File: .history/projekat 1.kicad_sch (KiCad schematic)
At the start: 224 parts, among them J1 Keyer, J2 audio_input, J3 Output signal, K1 Relay_SPST-NO_SSB (G6B-1177C(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, K2 Relay_SPST-NO_CW (G6B-1177C(-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, Q1 BC547, Q2 BC547, Q3 BC549, Q4 BC549, Q5 BC549, Q6 BC547, Q7 IRF510, Q9 BC547, SW1 on/off_12V, SW3 audio_SsbMorse_selektor, SW4 on/off_zujanje, SW5 keying_CW_SSB_selektor, SW6 selektor_modulacija, SW7 selektor_izlaza, U1 LM386, U10 OPA656UB, U11 L7806, U12 LM386, U13 OPA656UB, U14 OPA656UB, U15 OPA656UB, U2 LM358, U3 LM358, U4 LM358, U5 OPA656UB, U6 4N35, U7 OPA656UB, U8 OPA656UB, U9 OPA656UB

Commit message: rešen problem errora na pcb-u, replicirati rešenjesa J1 konektora na svim ostalim simbolima koji zadaju error.
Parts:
- removed J1: Keyer, Connector_PinHeader_2.54mm:PinHeader_1x02_P2.54mm_Vertical, symbol Connector_Audio:AudioJack2
- removed RV1: 100k, Resistor_SMD:R_1206_3216Metric_Pad1.30x1.75mm_HandSolder, symbol Device:R_Potentiometer
- added J1: Conn_01x02_Pin, Connector_PinHeader_2.54mm:PinHeader_1x02_P2.54mm_Vertical, symbol Connector:Conn_01x02_Pin
- added var_att_300mVrms2: 100k linear pot, Potentiometer_THT:Potentiometer_Bourns_3386W_Horizontal, symbol Device:R_Potentiometer
- K1, K2: footprint footprints:RELAY_G6B-1177P-ND_OMR -> (none)
- MC1496_mix2, MC1496_mod1: footprint Package_SO:SOIC-14-16_3.9x9.9mm_P1.27mm -> Package_SO:SOIC-14_3.9x8.7mm_P1.27mm
- R62: footprint Package_TO_SOT_THT:TO-220-3_Vertical -> Resistor_THT:R_Axial_DIN0516_L15.5mm_D5.0mm_P20.32mm_Horizontal
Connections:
- net GND: now also var_att_300mVrms2.3
- net at U6.2: now also J1.1 (Pin_1)
- net at SW4.2 (B): now also J1.2 (Pin_2)
- net at C27.2, U2.6 (-): now also var_att_300mVrms2.2
- net at R40.2, U2.1: now also var_att_300mVrms2.1
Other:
- note added: "rešiti footprint za otpornike na banpass-u"
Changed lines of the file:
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@@
 		)
 	)
+	(text "rešiti footprint za otpornike na banpass-u"
+		(exclude_from_sim no)
+		(at 554.99 322.072 0)
+		(effects
+			(font
+				(size 1.27 1.27)
+			)
+		)
+	)
 	(text "2nd order Chebyshev, direct coupled, shunt inductor"
 		(exclude_from_sim no)
@@
 			)
 		)
-		(property "Footprint" "footprints:RELAY_G6B-1177P-ND_OMR"
+		(property "Footprint" ""
 			(at 379.73 142.24 0)
 			(hide yes)
@@
 			)
 		)
-		(property "Footprint" "Package_TO_SOT_THT:TO-220-3_Vertical"
+		(property "Footprint" "Resistor_THT:R_Axial_DIN0516_L15.5mm_D5.0mm_P20.32mm_Horizontal"
 			(at 530.352 317.5 90)
 			(hide yes)
@@
 	)
 	(symbol
-		(lib_id "Connector_Audio:AudioJack2")
-		(at 19.05 299.72 0)
-		(unit 1)
-		(body_style 1)
-		(exclude_from_sim no)
-		(in_bom yes)
-		(on_board yes)
-		(in_pos_files yes)
-		(dnp no)
-		(fields_autoplaced yes)
-		(property "Reference" "J1"
-			(at 18.415 290.83 0)
-			(show_name no)
-			(do_not_autoplace no)
-			(effects
-				(font
-					(size 1.27 1.27)
-				)
-			)
-		)
-		(property "Value" "Keyer"
-			(at 18.415 293.37 0)
-			(show_name no)
-			(do_not_autoplace no)
-			(effects
-				(font
-					(size 1.27 1.27)
-				)
-			)
-		)
-		(property "Footprint" "Connector_PinHeader_2.54mm:PinHeader_1x02_P2.54mm_Vertical"
-			(at 19.05 299.72 0)
-			(hide yes)
-			(show_name no)
-			(do_not_autoplace no)
-			(effects
-				(font
-					(size 1.27 1.27)
-				)
-			)
-		)
-		(property "Datasheet" ""
-			(at 19.05 299.72 0)
-			(hide yes)
-			(show_name no)
-			(do_not_autoplace no)
-			(effects
-				(font
-					(size 1.27 1.27)
-				)
-			)
-		)
-		(property "Description" "Audio Jack, 2 Poles (Mono / TS)"
-			(at 19.05 299.72 0)
-			(hide yes)
-			(show_name no)
-			(do_not_autoplace no)
-			(effects
-				(font
-					(size 1.27 1.27)
-				)
-			)
-		)
-		(pin "S"
-		)
-		(pin "T"
-		)
-		(instances
-			(project "projekat 1"
-				(path "/74b4ec7a-02ca-4148-b3fb-b94fa07f486f"
-					(reference "J1")
-					(unit 1)
-				)
-			)
-		)
-	)
-	(symbol
 		(lib_id "Device:R")
 		(at 165.1 39.37 0)
@@
 	)
 	(symbol
-		(lib_id "Device:R_Potentiometer")
-		(at 55.88 223.52 0)
-		(unit 1)
-		(body_style 1)
-		(exclude_from_sim no)
-		(in_bom yes)
-		(on_board yes)
-		(in_pos_files yes)
-		(dnp no)
-		(fields_autoplaced yes)
-		(property "Reference" "RV1"
-			(at 53.34 222.2499 0)
-			(show_name no)
-			(do_not_autoplace no)
-			(effects
-				(font
-					(size 1.27 1.27)
-				)
-				(justify right)
-			)
-		)
-		(property "Value" "100k"
-			(at 53.34 224.7899 0)
-			(show_name no)
-			(do_not_autoplace no)
-			(effects
-				(font
-					(size 1.27 1.27)
-				)
-				(justify right)
-			)
-		)
-		(property "Footprint" "Resistor_SMD:R_1206_3216Metric_Pad1.30x1.75mm_HandSolder"
-			(at 55.88 223.52 0)
-			(hide yes)
-			(show_name no)
-			(do_not_autoplace no)
-			(effects
-				(font
-					(size 1.27 1.27)
-				)
-			)
-		)
-		(property "Datasheet" ""
-			(at 55.88 223.52 0)
-			(hide yes)
-			(show_name no)
-			(do_not_autoplace no)
-			(effects
-				(font
-					(size 1.27 1.27)
-				)
-			)
-		)
-		(property "Description" "Potentiometer"
-			(at 55.88 223.52 0)
-			(hide yes)
-			(show_name no)
-			(do_not_autoplace no)
-			(effects
-				(font
-					(size 1.27 1.27)
-				)
-			)
-		)
-		(property "Sim.Device" "R"
-			(at 55.88 223.52 0)
-			(hide yes)
-			(show_name no)
-			(do_not_autoplace no)
-			(effects
-				(font
-					(size 1.27 1.27)
-				)
-			)
-		)
-		(property "Sim.Type" "POT"
-			(at 55.88 223.52 0)
-			(hide yes)
-			(show_name no)
-			(do_not_autoplace no)
-			(effects
-				(font
-					(size 1.27 1.27)
-				)
-			)
-		)
-		(property "Sim.Pins" "1=r0 2=wiper 3=r1"
-			(at 55.88 223.52 0)
-			(hide yes)
-			(show_name no)
-			(do_not_autoplace no)
-			(effects
-				(font
-					(size 1.27 1.27)
-				)
-			)
-		)
-		(pin "2"
-		)
-		(pin "3"
-		)
-		(pin "1"
-		)
-		(instances
-			(project "projekat 1"
-				(path "/74b4ec7a-02ca-4148-b3fb-b94fa07f486f"
-					(reference "RV1")
-					(unit 1)
-				)
-			)
-		)
-	)
-	(symbol
 		(lib_id "Device:C")
 		(at 361.95 77.47 0)
@@
 			)
 		)
-		(property "Footprint" "Package_SO:SOIC-14-16_3.9x9.9mm_P1.27mm"
+		(property "Footprint" "Package_SO:SOIC-14_3.9x8.7mm_P1.27mm"
 			(at 130.81 132.08 0)
 			(hide yes)
@@
 			)
 		)
-		(property "Footprint" "Package_SO:SOIC-14-16_3.9x9.9mm_P1.27mm"
+		(property "Footprint" "Package_SO:SOIC-14_3.9x8.7mm_P1.27mm"
 			(at 128.27 45.72 0)
 			(hide yes)
@@
 	)
 	(symbol
+		(lib_id "Device:R_Potentiometer")
+		(at 55.88 223.52 0)
+		(unit 1)
+		(body_style 1)
+		(exclude_from_sim no)
+		(in_bom yes)
+		(on_board yes)
+		(in_pos_files yes)
+		(dnp no)
+		(property "Reference" "var_att_300mVrms2"
+			(at 49.53 223.52 90)
+			(show_name no)
+			(do_not_autoplace no)
+			(effects
+				(font
+					(size 1.27 1.27)
+				)
+			)
+		)
+		(property "Value" "100k linear pot"
+			(at 52.07 223.52 90)
+			(show_name no)
+			(do_not_autoplace no)
+			(effects
+				(font
+					(size 1.27 1.27)
+				)
+			)
+		)
+		(property "Footprint" "Potentiometer_THT:Potentiometer_Bourns_3386W_Horizontal"
+			(at 55.88 223.52 0)
+			(hide yes)
+			(show_name no)
+			(do_not_autoplace no)
+			(effects
+				(font
+					(size 1.27 1.27)
+				)
+			)
+		)
+		(property "Datasheet" ""
+			(at 55.88 223.52 0)
+			(hide yes)
+			(show_name no)
+			(do_not_autoplace no)
+			(effects
+				(font
+					(size 1.27 1.27)
+				)
+			)
+		)
+		(property "Description" "Potentiometer"
+			(at 55.88 223.52 0)
+			(hide yes)
+			(show_name no)
+			(do_not_autoplace no)
+			(effects
+				(font
+					(size 1.27 1.27)
+				)
+			)
+		)
+		(property "Sim.Device" "R"
+			(at 55.88 223.52 0)
+			(hide yes)
+			(show_name no)
+			(do_not_autoplace no)
+			(effects
+				(font
+					(size 1.27 1.27)
+				)
+			)
+		)
+		(property "Sim.Type" "POT"
+			(at 55.88 223.52 0)
+			(hide yes)
+			(show_name no)
+			(do_not_autoplace no)
+			(effects
+				(font
+					(size 1.27 1.27)
+				)
+			)
+		)
+		(property "Sim.Pins" "1=r0 2=wiper 3=r1"
+			(at 55.88 223.52 0)
+			(hide yes)
+			(show_name no)
+			(do_not_autoplace no)
+			(effects
+				(font
+					(size 1.27 1.27)
+				)
+			)
+		)
+		(pin "3"
+		)
+		(pin "2"
+		)
+		(pin "1"
+		)
+		(instances
+			(project "projekat 1"
+				(path "/74b4ec7a-02ca-4148-b3fb-b94fa07f486f"
+					(reference "var_att_300mVrms2")
+					(unit 1)
+				)
+			)
+		)
+	)
+	(symbol
 		(lib_id "Device:R")
 		(at 284.48 77.47 0)
@@
 	)
 	(symbol
+		(lib_id "Connector:Conn_01x02_Pin")
+		(at 19.05 297.18 0)
+		(unit 1)
+		(body_style 1)
+		(exclude_from_sim no)
+		(in_bom yes)
+		(on_board yes)
+		(in_pos_files yes)
+		(dnp no)
+		(fields_autoplaced yes)
+		(property "Reference" "J1"
+			(at 19.685 292.1 0)
+			(show_name no)
+			(do_not_autoplace no)
+			(effects
+				(font
+					(size 1.27 1.27)
+				)
+			)
+		)
+		(property "Value" "Conn_01x02_Pin"
+			(at 19.685 294.64 0)
+			(show_name no)
+			(do_not_autoplace no)
+			(effects
+				(font
+					(size 1.27 1.27)
+				)
+			)
+		)
+		(property "Footprint" "Connector_PinHeader_2.54mm:PinHeader_1x02_P2.54mm_Vertical"
+			(at 19.05 297.18 0)
+			(hide yes)
+			(show_name no)
+			(do_not_autoplace no)
+			(effects
+				(font
+					(size 1.27 1.27)
+				)
+			)
+		)
+		(property "Datasheet" ""
+			(at 19.05 297.18 0)
+			(hide yes)
+			(show_name no)
+			(do_not_autoplace no)
+			(effects
+				(font
+					(size 1.27 1.27)
+				)
+			)
+		)
+		(property "Description" "Generic connector, single row, 01x02, script generated"
+			(at 19.05 297.18 0)
+			(hide yes)
+			(show_name no)
+			(do_not_autoplace no)
+			(effects
+				(font
+					(size 1.27 1.27)
+				)
+			)
+		)
+		(pin "2"
+		)
+		(pin "1"
+		)
+		(instances
+			(project "projekat 1"
+				(path "/74b4ec7a-02ca-4148-b3fb-b94fa07f486f"
+					(reference "J1")
+					(unit 1)
+				)
+			)
+		)
+	)
+	(symbol
 		(lib_id "Device:L")
 		(at 494.03 311.15 90)
@@
 			)
 		)
-		(property "Footprint" "footprints:RELAY_G6B-1177P-ND_OMR"
+		(property "Footprint" ""
 			(at 346.71 142.24 0)
 			(hide yes)

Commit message: organizovan layout tone generation, signal input, headphone interface. Promenjen net na LE diodi u 12V_supply_1 i dodat otpornik od 500 oma.
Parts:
- removed J2: audio_input, Connector_PinHeader_2.54mm:PinHeader_1x02_P2.54mm_Vertical, symbol Connector_Audio:AudioJack2
- removed TS_6.35mm1: head_out, Connector_PinHeader_2.54mm:PinHeader_1x01_P2.54mm_Vertical, symbol Connector_Audio:AudioJack2
- added J2, J4: Conn_01x02_Pin, Connector_PinHeader_2.54mm:PinHeader_1x02_P2.54mm_Vertical, symbol Connector:Conn_01x02_Pin
- added R63: 500, Resistor_SMD:R_1206_3216Metric_Pad1.30x1.75mm_HandSolder, symbol Device:R
- BZ1: footprint Connector_PinHeader_2.54mm:PinHeader_1x01_P2.54mm_Vertical -> Connector_PinHeader_2.54mm:PinHeader_1x02_P2.54mm_Vertical
- SW4: footprint Connector_PinHeader_2.54mm:PinHeader_1x01_P2.54mm_Vertical -> Connector_PinHeader_2.54mm:PinHeader_1x03_P2.54mm_Vertical
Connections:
- net 12V_supply_1: now also R63.1
- net GND: now also J2.1 (Pin_1), J4.2 (Pin_2)
- net VCC: no longer D1.2 (A)
- net at C37.2: now also J2.2 (Pin_2)
- net at C38.1: now also J4.1 (Pin_1)
- new net: D1.2 (A), R63.2

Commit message: Izvršena prva korekcija layout-a tone generation, signal input, headphone interfacebloka, zamenjen footprint lm358 u SOIC-8. U sledećoj iteraciji dodati više slojeva, trace-ve koji su ispod komponenata spustiti u donji sloj, pregledati trace-ove
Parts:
- R63: value 500 -> 220
- U2, U3, U4: footprint Package_DIP:DIP-8_W7.62mm_LongPads -> Package_SO:SOIC-8_3.9x4.9mm_P1.27mm
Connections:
- net +6V: now also R63.1
- net 12V_supply_1: no longer R63.1
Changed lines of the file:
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@@
 	)
 	(label "12V_supply_1"
-		(at 25.4 274.32 0)
-		(effects
-			(font
-				(size 1.27 1.27)
-				(thickness 0.254)
-				(bold yes)
-				(italic yes)
-			)
-			(justify left bottom)
-		)
-	)
-	(label "12V_supply_1"
 		(at 210.82 320.04 270)
 		(effects
@@
 			)
 		)
-		(property "Footprint" "Package_DIP:DIP-8_W7.62mm_LongPads"
+		(property "Footprint" "Package_SO:SOIC-8_3.9x4.9mm_P1.27mm"
 			(at 114.3 242.57 0)
 			(hide yes)
@@
 			)
 		)
-		(property "Footprint" "Package_DIP:DIP-8_W7.62mm_LongPads"
+		(property "Footprint" "Package_SO:SOIC-8_3.9x4.9mm_P1.27mm"
 			(at 237.49 227.33 0)
 			(hide yes)
@@
 			)
 		)
-		(property "Footprint" "Package_DIP:DIP-8_W7.62mm_LongPads"
+		(property "Footprint" "Package_SO:SOIC-8_3.9x4.9mm_P1.27mm"
 			(at 149.86 281.94 0)
 			(hide yes)
@@
 			)
 		)
-		(property "Footprint" "Package_DIP:DIP-8_W7.62mm_LongPads"
+		(property "Footprint" "Package_SO:SOIC-8_3.9x4.9mm_P1.27mm"
 			(at 246.38 227.33 0)
 			(hide yes)
@@
 	)
 	(symbol
+		(lib_id "power:+6V")
+		(at 25.4 274.32 0)
+		(unit 1)
+		(body_style 1)
+		(exclude_from_sim no)
+		(in_bom yes)
+		(on_board yes)
+		(in_pos_files yes)
+		(dnp no)
+		(property "Reference" "#PWR016"
+			(at 25.4 278.13 0)
+			(hide yes)
+			(show_name no)
+			(do_not_autoplace no)
+			(effects
+				(font
+					(size 1.27 1.27)
+				)
+			)
+		)
+		(property "Value" "+6V"
+			(at 25.4 270.002 0)
+			(show_name no)
+			(do_not_autoplace no)
+			(effects
+				(font
+					(size 1.27 1.27)
+				)
+			)
+		)
+		(property "Footprint" ""
+			(at 25.4 274.32 0)
+			(hide yes)
+			(show_name no)
+			(do_not_autoplace no)
+			(effects
+				(font
+					(size 1.27 1.27)
+				)
+			)
+		)
+		(property "Datasheet" ""
+			(at 25.4 274.32 0)
+			(hide yes)
+			(show_name no)
+			(do_not_autoplace no)
+			(effects
+				(font
+					(size 1.27 1.27)
+				)
+			)
+		)
+		(property "Description" "Power symbol creates a global label with name \"+6V\""
+			(at 25.4 274.32 0)
+			(hide yes)
+			(show_name no)
+			(do_not_autoplace no)
+			(effects
+				(font
+					(size 1.27 1.27)
+				)
+			)
+		)
+		(pin "1"
+		)
+		(instances
+			(project "projekat 1"
+				(path "/74b4ec7a-02ca-4148-b3fb-b94fa07f486f"
+					(reference "#PWR016")
+					(unit 1)
+				)
+			)
+		)
+	)
+	(symbol
 		(lib_id "Device:C_Polarized_US")
 		(at 110.49 72.39 0)
@@
 			)
 		)
-		(property "Footprint" "Package_DIP:DIP-8_W7.62mm_LongPads"
+		(property "Footprint" "Package_SO:SOIC-8_3.9x4.9mm_P1.27mm"
 			(at 69.85 226.06 0)
 			(hide yes)
@@
 			)
 		)
-		(property "Footprint" "Package_DIP:DIP-8_W7.62mm_LongPads"
+		(property "Footprint" "Package_SO:SOIC-8_3.9x4.9mm_P1.27mm"
 			(at 41.91 226.06 0)
 			(hide yes)
@@
 			)
 		)
-		(property "Footprint" "Package_DIP:DIP-8_W7.62mm_LongPads"
+		(property "Footprint" "Package_SO:SOIC-8_3.9x4.9mm_P1.27mm"
 			(at 172.72 266.7 0)
 			(hide yes)
@@
 			)
 		)
-		(property "Value" "500"
+		(property "Value" "220"
 			(at 27.94 279.3999 0)
 			(show_name no)
@@
 			)
 		)
-		(property "Footprint" "Package_DIP:DIP-8_W7.62mm_LongPads"
+		(property "Footprint" "Package_SO:SOIC-8_3.9x4.9mm_P1.27mm"
 			(at 157.48 213.36 0)
 			(hide yes)
@@
 		(in_pos_files yes)
 		(dnp no)
-		(fields_autoplaced yes)
 		(property "Reference" "#PWR03"
 			(at 361.95 72.39 0)
@@
 		)
 		(property "Value" "+6V"
-			(at 361.95 63.5 0)
+			(at 361.95 64.262 0)
 			(show_name no)
 			(do_not_autoplace no)
@@
 			)
 		)
-		(property "Footprint" "Package_DIP:DIP-8_W7.62mm_LongPads"
+		(property "Footprint" "Package_SO:SOIC-8_3.9x4.9mm_P1.27mm"
 			(at 228.6 227.33 0)
 			(hide yes)

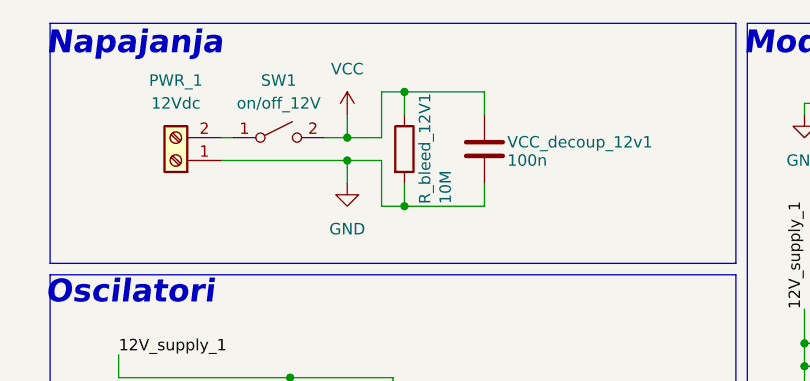
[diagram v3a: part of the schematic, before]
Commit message: dorađen layout pcb-a, dodati novi layeri, sprovedene vije.
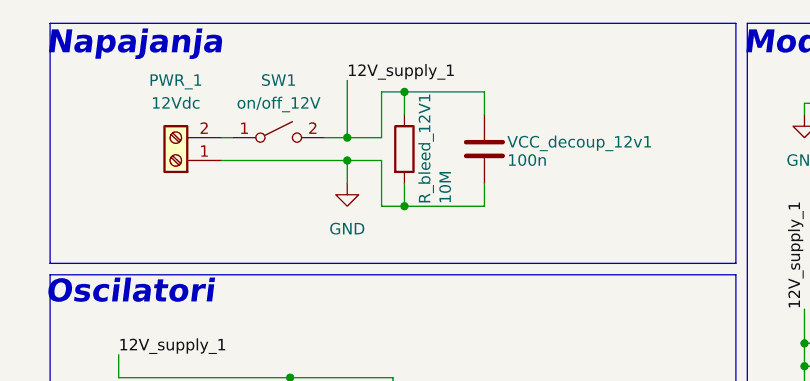
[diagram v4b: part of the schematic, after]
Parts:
- PWR_1, SW1: footprint Connector_PinHeader_2.54mm:PinHeader_1x01_P2.54mm_Vertical -> Connector_PinHeader_2.54mm:PinHeader_1x02_P2.54mm_Vertical
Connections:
- net 12V_supply_1: now also R_bleed_12V1.1, SW1.2 (B), VCC_decoup_12v1.1
- net VCC: no longer R_bleed_12V1.1, SW1.2 (B), VCC_decoup_12v1.1
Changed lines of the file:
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@@
 	(wire
 		(pts
+			(xy 45.72 19.05) (xy 45.72 25.4)
+		)
+		(stroke
+			(width 0)
+			(type default)
+		)
+	)
+	(wire
+		(pts
 			(xy 355.6 125.73) (xy 358.14 125.73)
 		)
@@
 	(wire
 		(pts
-			(xy 45.72 25.4) (xy 45.72 22.86)
-		)
-		(stroke
-			(width 0)
-			(type default)
-		)
-	)
-	(wire
-		(pts
 			(xy 161.29 33.02) (xy 161.29 43.18)
 		)
@@
 		)
 	)
+	(label "12V_supply_1"
+		(at 45.72 19.05 0)
+		(effects
+			(font
+				(size 1.27 1.27)
+			)
+			(justify left bottom)
+		)
+	)
 	(label "output_amplification_cw"
 		(at 350.52 248.92 180)
@@
 			)
 		)
-		(property "Footprint" "Connector_PinHeader_2.54mm:PinHeader_1x01_P2.54mm_Vertical"
+		(property "Footprint" "Connector_PinHeader_2.54mm:PinHeader_1x02_P2.54mm_Vertical"
 			(at 38.1 25.4 0)
 			(hide yes)
@@
 			)
 		)
-		(property "Footprint" "Connector_PinHeader_2.54mm:PinHeader_1x01_P2.54mm_Vertical"
+		(property "Footprint" "Connector_PinHeader_2.54mm:PinHeader_1x02_P2.54mm_Vertical"
 			(at 26.67 27.94 0)
 			(hide yes)
@@
 					(unit 1)
 				)
-			)
-		)
-	)
-	(symbol
-		(lib_id "power:VCC")
-		(at 45.72 22.86 0)
-		(unit 1)
-		(body_style 1)
-		(exclude_from_sim no)
-		(in_bom yes)
-		(on_board yes)
-		(in_pos_files yes)
-		(dnp no)
-		(fields_autoplaced yes)
-		(property "Reference" "#PWR013"
-			(at 45.72 26.67 0)
-			(hide yes)
-			(show_name no)
-			(do_not_autoplace no)
-			(effects
-				(font
-					(size 1.27 1.27)
-				)
-			)
-		)
-		(property "Value" "VCC"
-			(at 45.72 17.78 0)
-			(show_name no)
-			(do_not_autoplace no)
-			(effects
-				(font
-					(size 1.27 1.27)
-				)
-			)
-		)
-		(property "Footprint" ""
-			(at 45.72 22.86 0)
-			(hide yes)
-			(show_name no)
-			(do_not_autoplace no)
-			(effects
-				(font
-					(size 1.27 1.27)
-				)
-			)
-		)
-		(property "Datasheet" ""
-			(at 45.72 22.86 0)
-			(hide yes)
-			(show_name no)
-			(do_not_autoplace no)
-			(effects
-				(font
-					(size 1.27 1.27)
-				)
-			)
-		)
-		(property "Description" "Power symbol creates a global label with name \"VCC\""
-			(at 45.72 22.86 0)
-			(hide yes)
-			(show_name no)
-			(do_not_autoplace no)
-			(effects
-				(font
-					(size 1.27 1.27)
-				)
-			)
-		)
-		(pin "1"
-		)
-		(instances
-			(project "projekat 1"
-				(path "/74b4ec7a-02ca-4148-b3fb-b94fa07f486f"
-					(reference "#PWR013")
-					(unit 1)
-				)

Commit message: Dodati decoupling koncdnzatori na sve blokove i operacione, obrisan gornji layer bakra, sve vije prebačene na through, drc zadaje erore da su netovi šortivani
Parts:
- added VCC_decoup_12v2, VCC_decoup_12v3, VCC_decoup_12v4, VCC_decoup_12v5, VCC_decoup_12v6, VCC_decoup_12v7, VCC_decoup_12v8, VCC_decoup_12v9: 100n, Capacitor_SMD:C_1206_3216Metric, symbol Device:C
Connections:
- net 12V_supply_1: now also VCC_decoup_12v2.1, VCC_decoup_12v3.1, VCC_decoup_12v5.1, VCC_decoup_12v6.1, VCC_decoup_12v7.1, VCC_decoup_12v8.1, VCC_decoup_12v9.1
- net 12V_supply_CW: now also VCC_decoup_12v4.1
- net GND: now also VCC_decoup_12v2.2, VCC_decoup_12v3.2, VCC_decoup_12v4.2, VCC_decoup_12v5.2, VCC_decoup_12v6.2, VCC_decoup_12v7.2, VCC_decoup_12v8.2, VCC_decoup_12v9.2

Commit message: dodati footprinti za promenljive kondenzatore (proveriti da li su adekvatni)
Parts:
- removed C1, C2, C41, C42: 100p, Capacitor_SMD:C_1206_3216Metric, symbol Device:C
- removed C39, C40, decoup_+6V1: 100n, Capacitor_SMD:C_1206_3216Metric, symbol Device:C
- removed C_d_op1, C_d_op2, C_d_op3, C_d_op4, C_d_op5: 0,1u, Capacitor_SMD:C_1206_3216Metric, symbol Device:C
- removed C_d_op_2_1, C_d_op_2_2: 10n, Capacitor_SMD:C_1206_3216Metric, symbol Device:C
- removed C_dc1, C_dc2, C_lo_vfo1: 10nF, Capacitor_SMD:C_1206_3216Metric, symbol Device:C
- removed J3: Output signal, Connector_PinHeader_2.54mm:PinHeader_1x02_P2.54mm_Vertical, symbol Connector:Screw_Terminal_01x02
- removed K1: Relay_SPST-NO_SSB (G6B-1177C(-FD)-ND-US), symbol Relay:Relay_SPST-NO
- removed K2: Relay_SPST-NO_CW (G6B-1177C(-FD)-ND-US), symbol Relay:Relay_SPST-NO
- removed L1, L11, L5, L7: 1.6u, Inductor_SMD:L_1206_3216Metric, symbol Device:L
- removed L10, L3, L6, L8: 3.9u, Inductor_SMD:L_1206_3216Metric, symbol Device:L
- removed L4, L9: 750n, Capacitor_SMD:C_1206_3216Metric, symbol Device:L
- removed Q7: IRF510, Package_TO_SOT_THT:TO-220-3_Vertical, symbol Transistor_FET:IRF540N
- removed Q9: BC547, Package_TO_SOT_THT:TO-92_Inline, symbol Transistor_BJT:BC547
- removed R55, R56, R61: 50R, Package_TO_SOT_THT:TO-220-3_Vertical, symbol Device:R
- removed R57: R, Package_TO_SOT_THT:TO-220-3_Vertical, symbol Device:R
- removed R58, R59, R60, R_f3, R_filter_1, R_filter_2, R_in3: R, Resistor_SMD:R_1206_3216Metric_Pad1.30x1.75mm_HandSolder, symbol Device:R
- removed R62: 50R, Resistor_THT:R_Axial_DIN0516_L15.5mm_D5.0mm_P20.32mm_Horizontal, symbol Device:R
- removed R_f1: 127k, Resistor_SMD:R_1206_3216Metric_Pad1.30x1.75mm_HandSolder, symbol Device:R
- removed R_f2: 3k, Resistor_SMD:R_1206_3216Metric_Pad1.30x1.75mm_HandSolder, symbol Device:R
- removed R_in1: 1k, Package_TO_SOT_THT:TO-220-3_Vertical, symbol Device:R
- removed R_in2: 1k, Resistor_SMD:R_1206_3216Metric_Pad1.30x1.75mm_HandSolder, symbol Device:R
- removed SW6: selektor_modulacija, Connector_PinHeader_2.54mm:PinHeader_1x03_P2.54mm_Vertical, symbol Switch:SW_SPDT
- removed SW7: selektor_izlaza, Connector_PinHeader_2.54mm:PinHeader_1x03_P2.54mm_Vertical, symbol Switch:SW_SPDT
- removed U10, U13, U14, U15, U5, U7, U8, U9: OPA656UB, Package_SO:SOIC-8-1EP_3.9x4.9mm_P1.27mm_EP2.95x4.9mm_Mask2.34x2.34mm, symbol OPA656UB:OPA656UB
- removed U11: L7806, Package_TO_SOT_THT:TO-220-3_Vertical, symbol Regulator_Linear:L7806
- removed var_att1, var_att_100mVrms1, var_att_15mVrms1, var_att_60mVrms1: 1k linear pot, Potentiometer_THT:Potentiometer_Bourns_3386W_Horizontal, symbol Device:R_Potentiometer
- added SW2: SW_Nidec_CAS-120A1, Connector_PinHeader_2.54mm:PinHeader_1x03_P2.54mm_Vertical, symbol Switch:SW_Nidec_CAS-120A1
- C22, C23: footprint (none) -> Capacitor_SMD:C_Trimmer_Murata_TZB4-A
- C2_tune1, C2_tune2_1, C2_tune2_2: footprint Resistor_SMD:R_1206_3216Metric_Pad1.30x1.75mm_HandSolder -> Capacitor_SMD:C_Trimmer_Voltronics_JZ
- C2_tune3: footprint (none) -> Capacitor_SMD:C_Trimmer_Voltronics_JZ
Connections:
- net 12V_supply_1: now also SW2.2 (B); no longer R2.1, R3.1, R5.1, R6.1, VCC_decoup_12v2.1, VCC_decoup_12v3.1
- net 12V_supply_CW: now also SW2.3 (A)
- new net 12V_supply_2: R2.1, R3.1, R5.1, R6.1, SW2.1 (C), VCC_decoup_12v2.1, VCC_decoup_12v3.1
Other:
- note removed: "A_1 = 500/3,93 = 128,21"
- note removed: "A_2 = 1,5/0,5 = 3"
- note removed: "A_4(subfinal and out) = 15,8/1,5 = 10,53 (rec.)"
- note removed: "Calculate R values for 1.5 to 15.8 vrms"
- note removed: "Calculate output and A_3 for CW and R numbers"
- note removed: "rešiti footprint za otpornike na banpass-u"
